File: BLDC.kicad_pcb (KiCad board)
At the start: 4 copper layers, 60 x 60 mm, 120 parts, among them J1 43650-0510, J2 436500313, J3 TC2030-MCP-NL, J4 43650-0510, U1 LMZ21700SIL, U12 MCP9808, U13 AS5047U, U17 INA250, U18 INA250, U19 INA250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

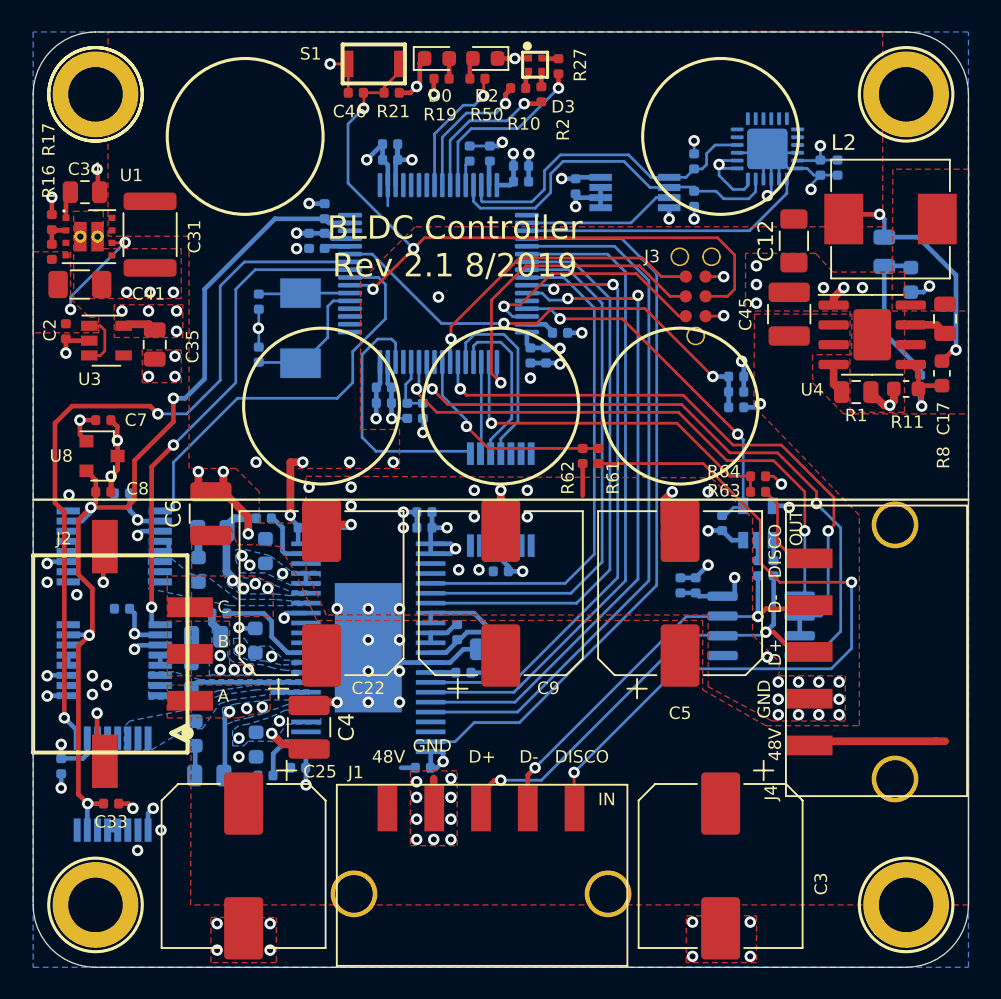
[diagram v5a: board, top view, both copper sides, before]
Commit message: consolidate lots of BOM line items, lots of clean up
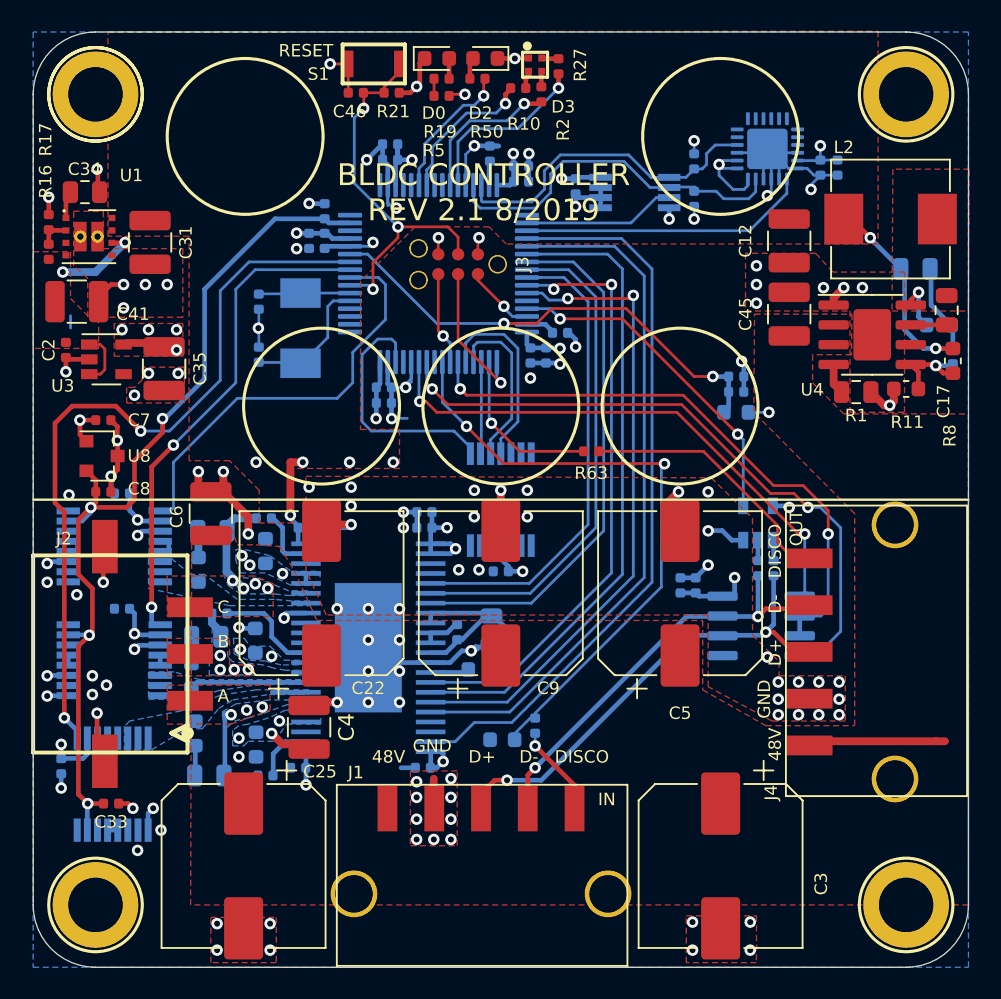
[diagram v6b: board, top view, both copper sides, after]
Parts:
- removed R3: 47.0kΩ, Resistor_SMD:R_0402_1005Metric
- removed R48: DNP, Resistor_SMD:R_0402_1005Metric
- removed R52: 10.0kΩ, Resistor_SMD:R_0402_1005Metric
- removed R56: 47k, Resistor_SMD:R_0402_1005Metric
- removed R64: 137.0kΩ, Resistor_SMD:R_0402_1005Metric
- added R5: 150R, Resistor_SMD:R_0402_1005Metric, F.Cu at (144.7, 79.1)
- C1, C32, C39, C42, C46, C50, C53, C56, C61, C62, C64, C68, C73: value 100.0nF -> 100n
- C12: value 4.7u -> 22u; footprint Capacitor_SMD:C_1206_3216Metric -> Capacitor_SMD:C_1210_3225Metric
- C15, C18, C2, C36, C52, C60: value 1.0μF -> 1u
- C20: value 100.0nF -> 1u
- C21: value 100nF -> 100n
- C22, C25, C3, C5, C9: value 180uF -> 100u
- C31: value 22μF -> 22u; footprint Capacitor_SMD:C_1812_4532Metric -> Capacitor_SMD:C_1210_3225Metric
- C34: value 3.3nF -> 2n2
- C35: value 22.0μF -> 22u; footprint Capacitor_SMD:C_0805_2012Metric -> Capacitor_SMD:C_1210_3225Metric
- C41: value 47.0μF -> 22u; footprint Capacitor_SMD:C_1206_3216Metric -> Capacitor_SMD:C_1210_3225Metric
- C54, C57: value 27p -> 16p
- L2: value 82 uH -> 82u
- R0, R15: value 39.2kΩ -> 49k9; footprint Resistor_SMD:R_0402_1005Metric -> Resistor_SMD:R_0603_1608Metric
- R10: value 150.0Ω -> 150R
- R16: value 681.0kΩ -> 681k
- R17: value 180.0kΩ -> 180k
- R19, R50: value 220.0Ω -> 150R
- R2: value 62.0Ω -> 150R
- R21, R55: value 2.21kΩ -> 2k21
- R27: value 180.0Ω -> 150R
- R32: value TBC -> 1R
- R4, R6: value 56.2Ω -> 56R2
- R61: value 28.7kΩ -> 2k21; moved to B.Cu
- R62: value 137.0kΩ -> 49k9; footprint Resistor_SMD:R_0402_1005Metric -> Resistor_SMD:R_0603_1608Metric; moved to B.Cu
- R63: value 28.7kΩ -> 2k21
- U7: value SN74LVC1G66DCKR -> SN74LVC1G66DBV
- moved R62 18.9 mm to (148.6, 120.4), turned to 180 degrees
- moved R61 17.8 mm to (150.7, 119.5)
- moved J3 13.5 mm to (148.3, 89.9), turned to 180 degrees
- moved R63 11.0 mm to (154.3, 101.9)
- moved R7 3.41 mm to (176.6, 93.8), turned to 180 degrees
- moved C10 2.70 mm to (177.5, 95.8)
- moved C11 2.28 mm to (175.1, 90.2), turned to 0 degrees
- moved C35 1.66 mm to (126.9, 96.6)
- moved R32 1.20 mm to (147.9, 113.4), turned to 270 degrees
- moved C2 1.20 mm to (120.6, 95.4)
- moved U3 1.20 mm to (123.2, 96.0)
- moved C41 1.12 mm to (121.3, 92.3), turned to 0 degrees
- moved R0 1.12 mm to (147.2, 115.9)
- moved R8 1.06 mm to (177.5, 96.1)
- moved C17 0.56 mm to (177.1, 92.8)
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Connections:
- net /ENC_ALIGN renamed Net-(U9-Pad44)
- C41 pad 1: GND -> /3V9
- C41 pad 2: /3V9 -> GND
- R19 pad 2: GND -> Net-(R19-Pad2)
- U9 pad 22: Net-(U9-Pad22) -> /LED_STATUS
- U9 pad 23: Net-(U9-Pad23) -> /LED_G
- U9 pad 24: /LED_STATUS -> Net-(U9-Pad24)
- U9 pad 25: /LED_G -> Net-(U9-Pad25)
- U9 pad 28: /BOOT2 -> GND
- U9 pad 60: /BOOT0 -> GND
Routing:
- net Net-(J1-Pad1): track 48.9 -> 5.88 mm, vias 2 -> 1
- net /DISCO_BUS_IN: track 13.8 -> 40.3 mm, vias 1 -> 2
- net /SWD_RESET: track 46.6 -> 25.1 mm
- net /SWD_SWO: track 19.7 -> 5.95 mm
- net /DISCO_BUS_OUT: track 23.0 -> 10.6 mm
- net /SWD_SWCLK: track 21.2 -> 9.53 mm
- net GND: track 125.0 -> 136.3 mm, vias 117 -> 120
- net Net-(J4-Pad1): track 7.01 -> 18.0 mm
- net /SWD_SWDIO: track 15.5 -> 4.70 mm
- net Net-(C10-Pad1): track 9.86 -> 5.39 mm
- net /BOOT0: track 3.83 -> 0.00 mm
- net +12V: track 34.7 -> 31.3 mm
- net /MOT_RST_B: track 36.1 -> 34.1 mm
- net /driver_DRV8312_AGND: track 15.5 -> 13.5 mm
- net Net-(C17-Pad1): track 1.36 -> 3.34 mm
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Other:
- board text added: "BLDC CONTROLLER REV 2.1 8/2019"
- board text added: "RESET"
- board text removed: "BLDC Controller Rev 2.1 8/2019"

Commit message: fix part numbers, move programming connector, add i2c test points
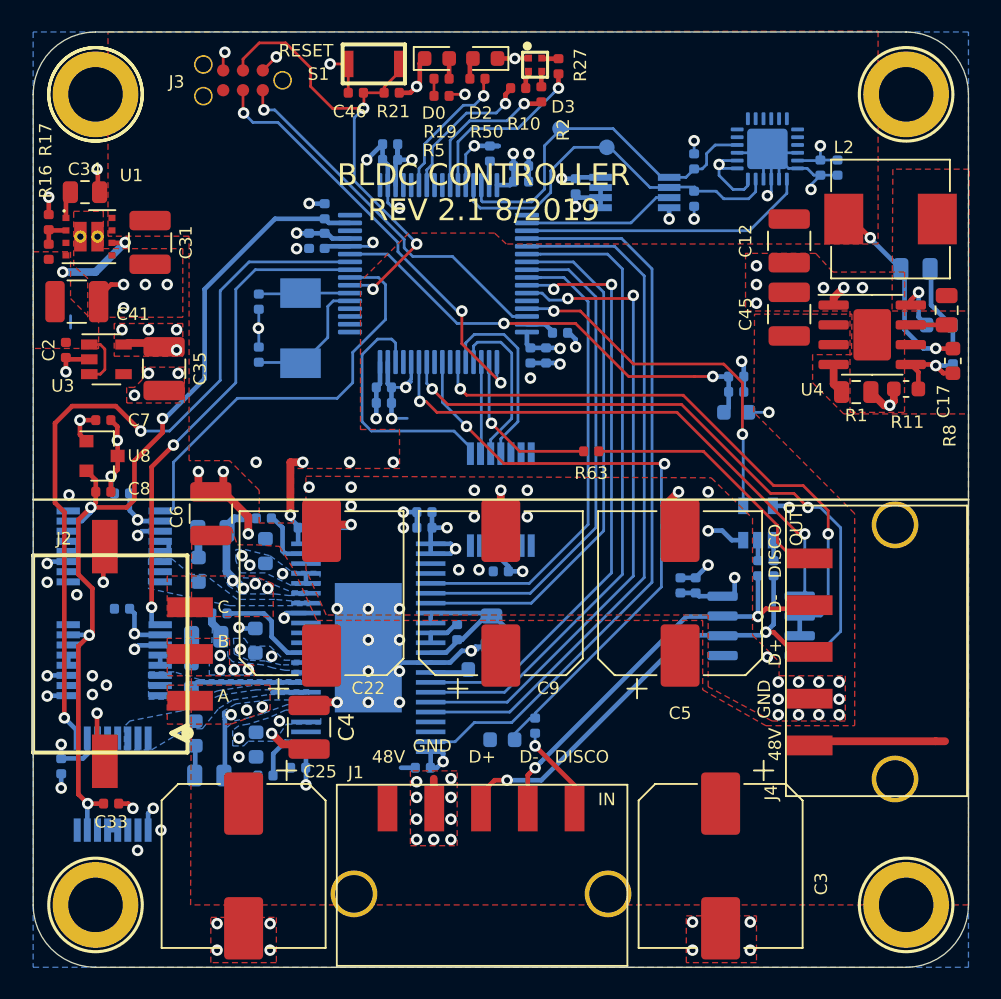
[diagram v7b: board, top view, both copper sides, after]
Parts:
- added TP1: TestPoint, TestPoint:TestPoint_Pad_D1.0mm, B.Cu at (152.3, 81.2)
- added TP2: TestPoint, TestPoint:TestPoint_Pad_D1.0mm, B.Cu at (155.3, 82.4)
- J3: value TC2030-MCP-NL -> DNP
- moved J3 18.2 mm to (134.5, 78.1)
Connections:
- U9 pad 55: /SWD_SWO -> Net-(U9-Pad55)
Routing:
- net /SWD_SWDIO: track 4.70 -> 24.0 mm
- net /SWD_SWCLK: track 9.53 -> 28.2 mm, vias 1 -> 3
- net /SWD_RESET: track 25.1 -> 32.2 mm
- net /SWD_SWO: track 5.95 -> 0.00 mm, vias 1 -> 0
- net /I2C_SDA: track 20.9 -> 23.2 mm
- net /RS485_SHUNT_EN: track 21.7 -> 23.9 mm
- net GND: track 136.3 -> 135.4 mm
- net /I2C_SCL: track 23.5 -> 24.4 mm
- net /VSENSE_VIN: track 30.6 -> 29.8 mm
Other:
- board text added: "SCL"
- board text added: "SDA"

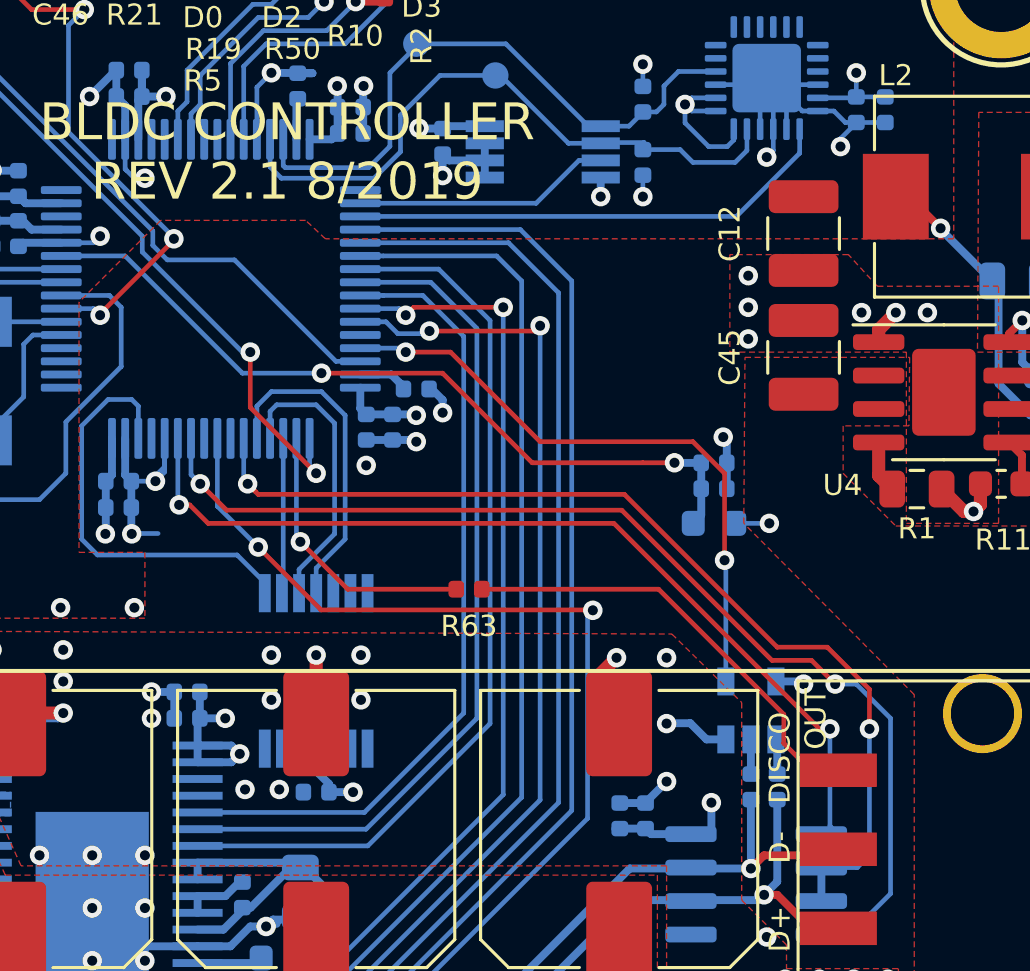
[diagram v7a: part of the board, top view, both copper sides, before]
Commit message: add test points to SPI bus
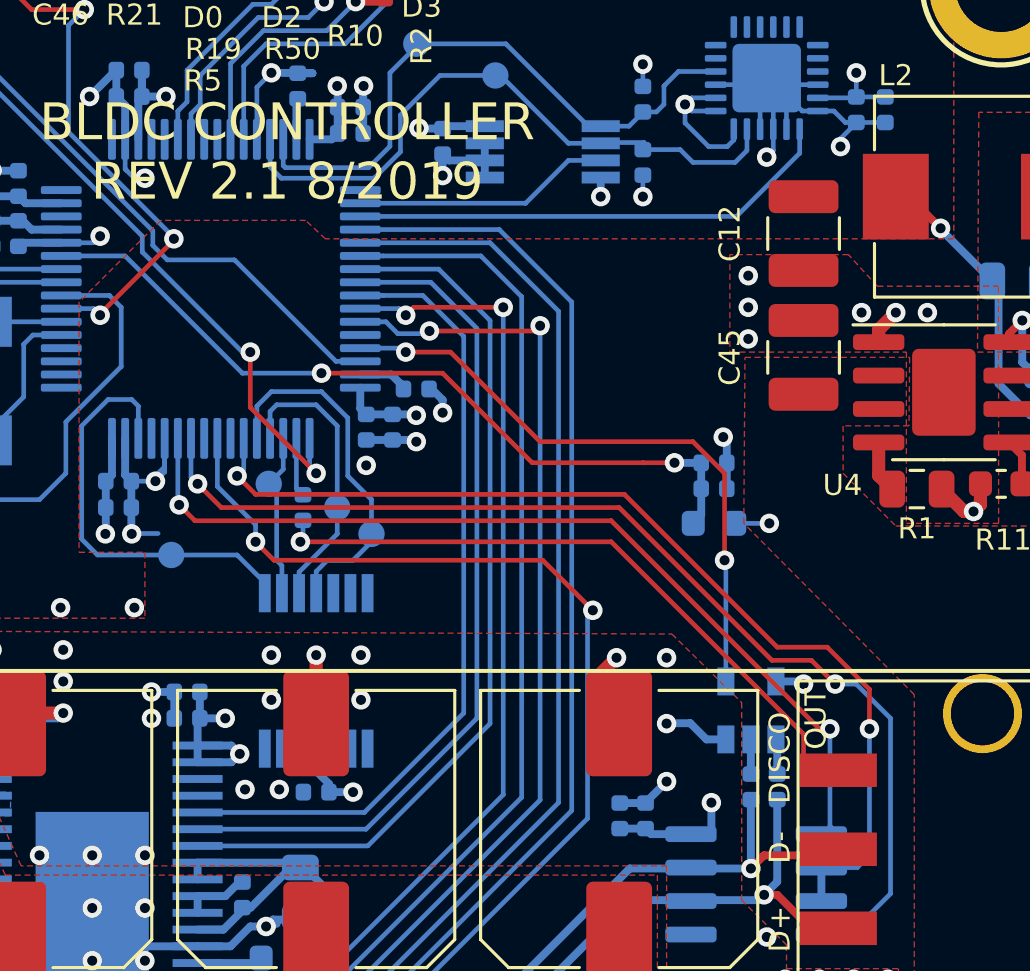
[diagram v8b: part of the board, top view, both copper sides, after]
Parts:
- added TP3: TestPoint, TestPoint:TestPoint_Pad_D1.0mm, B.Cu at (150.6, 99.8)
- added TP4: TestPoint, TestPoint:TestPoint_Pad_D1.0mm, B.Cu at (149.3, 98.8)
- added TP5: TestPoint, TestPoint:TestPoint_Pad_D1.0mm, B.Cu at (143.0, 100.6)
- added TP6: TestPoint, TestPoint:TestPoint_Pad_D1.0mm, B.Cu at (146.7, 97.9)
- R63: moved to B.Cu
- moved R63 7.02 mm to (148.0, 98.8), turned to 90 degrees
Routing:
- net Net-(J4-Pad1): track 18.0 -> 26.5 mm, vias 0 -> 1
- net /DISCO_BUS_OUT: track 10.6 -> 2.24 mm, vias 1 -> 0
- net /SPI_MOSI: track 12.4 -> 13.9 mm
- net /SPI_CLK: track 5.83 -> 6.45 mm
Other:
- board text added: "CS"
- board text added: "MISO"
- board text added: "MOSI"
- board text added: "SCK"
